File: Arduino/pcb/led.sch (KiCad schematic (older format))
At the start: 0 parts

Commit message: pcb: continue wiring / move parts to hierachival sheets
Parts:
- added C4: 100nF, symbol Device:C
- added D1: LED_RGB, symbol Device:LED_RGB
- added U2: 74HC595, SMD_Packages:SO-16-N, symbol floppyorgel-rescue:74HC595-74xx
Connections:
- new net: D1.4 (BA), U2.2 (QC)
- new net: D1.5 (GA), U2.1 (QB)
- new net: D1.6 (RA), U2.15 (QA)
- new net GND: C4.2, D1.1 (RK), D1.2 (GK), D1.3 (BK), U2.13 (G), U2.8 (GND)
- new net LATCH_LED: U2.12 (RCLK)
- new net MOSI: U2.14 (SER)
- new net SCK: U2.11 (SRCLK)
- new net VCC: C4.1, U2.10 (SRCLR), U2.16 (VCC)
- no-connect marks 0 -> 6
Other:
- note added: "Bypass"
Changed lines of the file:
@@
 $Descr A4 11693 8268
 encoding utf-8
-Sheet 1 6
+Sheet 5 6
 Title ""
 Date ""
@@
 Comment4 ""
 $EndDescr
+$Comp
+L power:VCC #PWR022
+U 1 1 5D09B29E
+P 5175 2850
+F 0 "#PWR022" H 5175 2700 50  0001 C CNN
+F 1 "VCC" H 5192 3023 50  0000 C CNN
+F 2 "" H 5175 2850 50  0001 C CNN
+F 3 "" H 5175 2850 50  0001 C CNN
+	1    5175 2850
+	1    0    0    -1
+$EndComp
+$Comp
+L power:GND #PWR023
+U 1 1 5D09B2A4
+P 5175 3950
+F 0 "#PWR023" H 5175 3700 50  0001 C CNN
+F 1 "GND" H 5180 3777 50  0000 C CNN
+F 2 "" H 5175 3950 50  0001 C CNN
+F 3 "" H 5175 3950 50  0001 C CNN
+	1    5175 3950
+	1    0    0    -1
+$EndComp
+$Comp
+L Device:LED_RGB D1
+U 1 1 5D09B2AA
+P 6700 3050
+F 0 "D1" H 6700 3547 50  0000 C CNN
+F 1 "LED_RGB" H 6700 3456 50  0000 C CNN
+F 2 "" H 6700 3000 50  0001 C CNN
+F 3 "~" H 6700 3000 50  0001 C CNN
+	1    6700 3050
+	-1   0    0    -1
+$EndComp
+$Comp
+L power:GND #PWR024
+U 1 1 5D09B2B0
+P 6900 3625
+F 0 "#PWR024" H 6900 3375 50  0001 C CNN
+F 1 "GND" H 6905 3452 50  0000 C CNN
+F 2 "" H 6900 3625 50  0001 C CNN
+F 3 "" H 6900 3625 50  0001 C CNN
+	1    6900 3625
+	1    0    0    -1
+$EndComp
+Wire Wire Line
+	6175 2950 6500 2950
+Wire Wire Line
+	6175 3050 6500 3050
+Connection ~ 6900 3050
+Connection ~ 6900 3250
+Wire Wire Line
+	6500 2950 6500 2850
+Wire Wire Line
+	6900 3050 6900 3250
+Wire Wire Line
+	6900 3250 6900 3625
+Wire Wire Line
+	6500 3150 6500 3250
+Wire Wire Line
+	6175 3150 6500 3150
+Wire Wire Line
+	6900 2850 6900 3050
+$Comp
+L power:GND #PWR021
+U 1 1 5D09B2C0
+P 4775 3550
+F 0 "#PWR021" H 4775 3300 50  0001 C CNN
+F 1 "GND" H 4780 3377 50  0000 C CNN
+F 2 "" H 4775 3550 50  0001 C CNN
+F 3 "" H 4775 3550 50  0001 C CNN
+	1    4775 3550
+	1    0    0    -1
+$EndComp
+Wire Wire Line
+	4775 3250 4375 3250
+$Comp
+L power:VCC #PWR020
+U 1 1 5D09B2C7
+P 4375 2850
+F 0 "#PWR020" H 4375 2700 50  0001 C CNN
+F 1 "VCC" H 4392 3023 50  0000 C CNN
+F 2 "" H 4375 2850 50  0001 C CNN
+F 3 "" H 4375 2850 50  0001 C CNN
+	1    4375 2850
+	1    0    0    -1
+$EndComp
+NoConn ~ 6175 3250
+NoConn ~ 6175 3350
+NoConn ~ 6175 3450
+NoConn ~ 6175 3550
+NoConn ~ 6175 3650
+NoConn ~ 6175 3850
+$Comp
+L floppyorgel-rescue:74HC595-74xx U2
+U 1 1 5D09B2D3
+P 5475 3400
+F 0 "U2" H 5625 4000 50  0000 C CNN
+F 1 "74HC595" H 5475 2800 50  0000 C CNN
+F 2 "SMD_Packages:SO-16-N" H 5475 3400 50  0001 C CNN
+F 3 "" H 5475 3400 50  0001 C CNN
+	1    5475 3400
+	1    0    0    -1
+$EndComp
+Wire Wire Line
+	4375 2850 4375 3250
+Text HLabel 4775 2950 0    50   Input ~ 0
+MOSI
+Text HLabel 4775 3150 0    50   Input ~ 0
+SCK
+Text HLabel 4775 3450 0    50   Input ~ 0
+LATCH_LED
+$Comp
+L Device:C C?
+U 1 1 5D18829B
+P 3750 3275
+AR Path="/5D18829B" Ref="C?"  Part="1"
+AR Path="/5CCFEC3E/5D18829B" Ref="C?"  Part="1"
+AR Path="/5CD3FBA6/5D18829B" Ref="C4"  Part="1"
+F 0 "C4" H 3525 3475 50  0000 L CNN
+F 1 "100nF" H 3475 3375 50  0000 L CNN
+F 2 "" H 3788 3125 50  0001 C CNN
+F 3 "~" H 3750 3275 50  0001 C CNN
+	1    3750 3275
+	1    0    0    -1
+$EndComp
+$Comp
+L power:VCC #PWR?
+U 1 1 5D1882A1
+P 3750 3000
+AR Path="/5CCFEC3E/5D1882A1" Ref="#PWR?"  Part="1"
+AR Path="/5CD3FBA6/5D1882A1" Ref="#PWR018"  Part="1"
+F 0 "#PWR018" H 3750 2850 50  0001 C CNN
+F 1 "VCC" H 3767 3173 50  0000 C CNN
+F 2 "" H 3750 3000 50  0001 C CNN
+F 3 "" H 3750 3000 50  0001 C CNN
+	1    3750 3000
+	1    0    0    -1
+$EndComp
+$Comp
+L power:GND #PWR?
+U 1 1 5D1882A7
+P 3750 3525
+AR Path="/5CCFEC3E/5D1882A7" Ref="#PWR?"  Part="1"
+AR Path="/5CD3FBA6/5D1882A7" Ref="#PWR019"  Part="1"
+F 0 "#PWR019" H 3750 3275 50  0001 C CNN
+F 1 "GND" H 3755 3352 50  0000 C CNN
+F 2 "" H 3750 3525 50  0001 C CNN
+F 3 "" H 3750 3525 50  0001 C CNN
+	1    3750 3525
+	1    0    0    -1
+$EndComp
+Wire Wire Line
+	3750 3000 3750 3125
+Wire Wire Line
+	3750 3425 3750 3525
+Text Notes 3375 2950 0    50   ~ 0
+Bypass
 $EndSCHEMATC

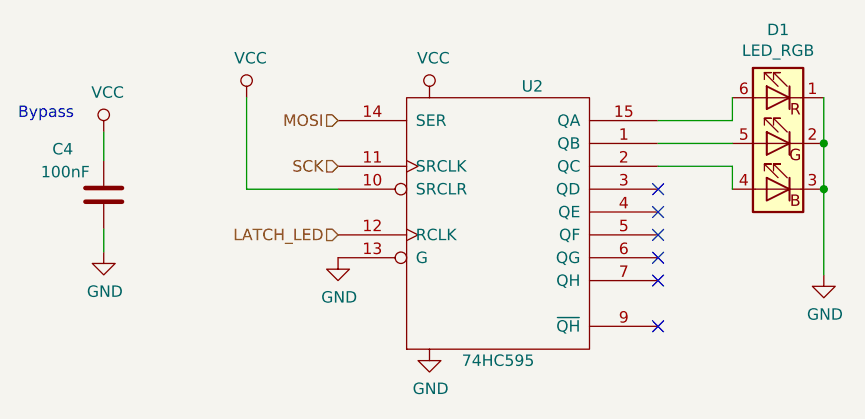
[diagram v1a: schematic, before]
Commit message: pcb: finish wiring / use ws2812 under chip led
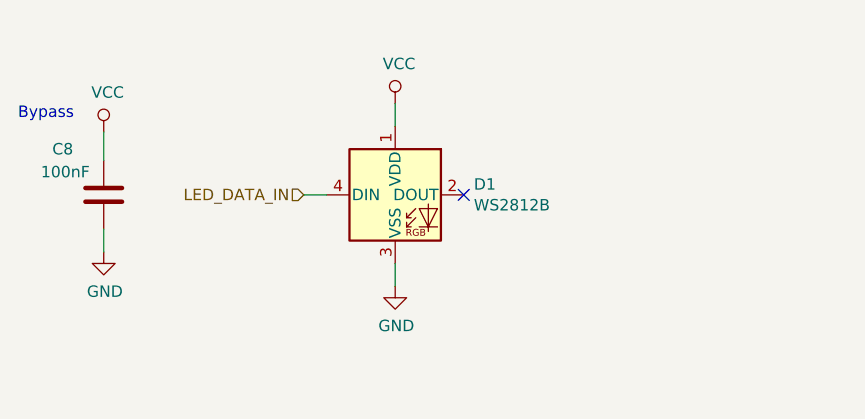
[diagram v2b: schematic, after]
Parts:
- removed D1: LED_RGB, symbol Device:LED_RGB
- removed U2: 74HC595, SMD_Packages:SO-16-N, symbol floppyorgel-rescue:74HC595-74xx
- added D1: WS2812B, LED_SMD:LED_WS2812B_PLCC4_5.0x5.0mm_P3.2mm, symbol LED:WS2812B
- renumbered C4 to C8
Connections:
- net GND: now also D1.3 (VSS)
- net VCC: now also D1.1 (VDD)
- new net LED_DATA_IN: D1.4 (DIN)
- no-connect marks 6 -> 1
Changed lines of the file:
@@
 $Descr A4 11693 8268
 encoding utf-8
-Sheet 5 6
+Sheet 6 6
 Title ""
 Date ""
@@
 $EndDescr
 $Comp
-L power:VCC #PWR022
-U 1 1 5D09B29E
-P 5175 2850
-F 0 "#PWR022" H 5175 2700 50  0001 C CNN
-F 1 "VCC" H 5192 3023 50  0000 C CNN
-F 2 "" H 5175 2850 50  0001 C CNN
-F 3 "" H 5175 2850 50  0001 C CNN
-	1    5175 2850
-	1    0    0    -1
-$EndComp
-$Comp
-L power:GND #PWR023
-U 1 1 5D09B2A4
-P 5175 3950
-F 0 "#PWR023" H 5175 3700 50  0001 C CNN
-F 1 "GND" H 5180 3777 50  0000 C CNN
-F 2 "" H 5175 3950 50  0001 C CNN
-F 3 "" H 5175 3950 50  0001 C CNN
-	1    5175 3950
-	1    0    0    -1
-$EndComp
-$Comp
-L Device:LED_RGB D1
-U 1 1 5D09B2AA
-P 6700 3050
-F 0 "D1" H 6700 3547 50  0000 C CNN
-F 1 "LED_RGB" H 6700 3456 50  0000 C CNN
-F 2 "" H 6700 3000 50  0001 C CNN
-F 3 "~" H 6700 3000 50  0001 C CNN
-	1    6700 3050
-	-1   0    0    -1
-$EndComp
-$Comp
-L power:GND #PWR024
-U 1 1 5D09B2B0
-P 6900 3625
-F 0 "#PWR024" H 6900 3375 50  0001 C CNN
-F 1 "GND" H 6905 3452 50  0000 C CNN
-F 2 "" H 6900 3625 50  0001 C CNN
-F 3 "" H 6900 3625 50  0001 C CNN
-	1    6900 3625
-	1    0    0    -1
-$EndComp
-Wire Wire Line
-	6175 2950 6500 2950
-Wire Wire Line
-	6175 3050 6500 3050
-Connection ~ 6900 3050
-Connection ~ 6900 3250
-Wire Wire Line
-	6500 2950 6500 2850
-Wire Wire Line
-	6900 3050 6900 3250
-Wire Wire Line
-	6900 3250 6900 3625
-Wire Wire Line
-	6500 3150 6500 3250
-Wire Wire Line
-	6175 3150 6500 3150
-Wire Wire Line
-	6900 2850 6900 3050
-$Comp
-L power:GND #PWR021
-U 1 1 5D09B2C0
-P 4775 3550
-F 0 "#PWR021" H 4775 3300 50  0001 C CNN
-F 1 "GND" H 4780 3377 50  0000 C CNN
-F 2 "" H 4775 3550 50  0001 C CNN
-F 3 "" H 4775 3550 50  0001 C CNN
-	1    4775 3550
-	1    0    0    -1
-$EndComp
-Wire Wire Line
-	4775 3250 4375 3250
-$Comp
-L power:VCC #PWR020
-U 1 1 5D09B2C7
-P 4375 2850
-F 0 "#PWR020" H 4375 2700 50  0001 C CNN
-F 1 "VCC" H 4392 3023 50  0000 C CNN
-F 2 "" H 4375 2850 50  0001 C CNN
-F 3 "" H 4375 2850 50  0001 C CNN
-	1    4375 2850
-	1    0    0    -1
-$EndComp
-NoConn ~ 6175 3250
-NoConn ~ 6175 3350
-NoConn ~ 6175 3450
-NoConn ~ 6175 3550
-NoConn ~ 6175 3650
-NoConn ~ 6175 3850
-$Comp
-L floppyorgel-rescue:74HC595-74xx U2
-U 1 1 5D09B2D3
-P 5475 3400
-F 0 "U2" H 5625 4000 50  0000 C CNN
-F 1 "74HC595" H 5475 2800 50  0000 C CNN
-F 2 "SMD_Packages:SO-16-N" H 5475 3400 50  0001 C CNN
-F 3 "" H 5475 3400 50  0001 C CNN
-	1    5475 3400
-	1    0    0    -1
-$EndComp
-Wire Wire Line
-	4375 2850 4375 3250
-Text HLabel 4775 2950 0    50   Input ~ 0
-MOSI
-Text HLabel 4775 3150 0    50   Input ~ 0
-SCK
-Text HLabel 4775 3450 0    50   Input ~ 0
-LATCH_LED
-$Comp
 L Device:C C?
 U 1 1 5D18829B
@@
 AR Path="/5D18829B" Ref="C?"  Part="1"
 AR Path="/5CCFEC3E/5D18829B" Ref="C?"  Part="1"
-AR Path="/5CD3FBA6/5D18829B" Ref="C4"  Part="1"
-F 0 "C4" H 3525 3475 50  0000 L CNN
+AR Path="/5CD3FBA6/5D18829B" Ref="C8"  Part="1"
+F 0 "C8" H 3525 3475 50  0000 L CNN
 F 1 "100nF" H 3475 3375 50  0000 L CNN
 F 2 "" H 3788 3125 50  0001 C CNN
@@
 P 3750 3000
 AR Path="/5CCFEC3E/5D1882A1" Ref="#PWR?"  Part="1"
-AR Path="/5CD3FBA6/5D1882A1" Ref="#PWR018"  Part="1"
-F 0 "#PWR018" H 3750 2850 50  0001 C CNN
+AR Path="/5CD3FBA6/5D1882A1" Ref="#PWR027"  Part="1"
+F 0 "#PWR027" H 3750 2850 50  0001 C CNN
 F 1 "VCC" H 3767 3173 50  0000 C CNN
 F 2 "" H 3750 3000 50  0001 C CNN
@@
 P 3750 3525
 AR Path="/5CCFEC3E/5D1882A7" Ref="#PWR?"  Part="1"
-AR Path="/5CD3FBA6/5D1882A7" Ref="#PWR019"  Part="1"
-F 0 "#PWR019" H 3750 3275 50  0001 C CNN
+AR Path="/5CD3FBA6/5D1882A7" Ref="#PWR028"  Part="1"
+F 0 "#PWR028" H 3750 3275 50  0001 C CNN
 F 1 "GND" H 3755 3352 50  0000 C CNN
 F 2 "" H 3750 3525 50  0001 C CNN
@@
 Text Notes 3375 2950 0    50   ~ 0
 Bypass
+$Comp
+L LED:WS2812B D1
+U 1 1 5CC4A8E5
+P 5025 3275
+F 0 "D1" H 5369 3321 50  0000 L CNN
+F 1 "WS2812B" H 5369 3230 50  0000 L CNN
+F 2 "LED_SMD:LED_WS2812B_PLCC4_5.0x5.0mm_P3.2mm" H 5075 2975 50  0001 L TNN
+F 3 "https://cdn-shop.adafruit.com/datasheets/WS2812B.pdf" H 5125 2900 50  0001 L TNN
+	1    5025 3275
+	1    0    0    -1
+$EndComp
+$Comp
+L power:VCC #PWR?
+U 1 1 5CC4D6AB
+P 5025 2875
+AR Path="/5CCFEC3E/5CC4D6AB" Ref="#PWR?"  Part="1"
+AR Path="/5CD3FBA6/5CC4D6AB" Ref="#PWR029"  Part="1"
+F 0 "#PWR029" H 5025 2725 50  0001 C CNN
+F 1 "VCC" H 5042 3048 50  0000 C CNN
+F 2 "" H 5025 2875 50  0001 C CNN
+F 3 "" H 5025 2875 50  0001 C CNN
+	1    5025 2875
+	1    0    0    -1
+$EndComp
+Wire Wire Line
+	5025 2875 5025 2975
+$Comp
+L power:GND #PWR030
+U 1 1 5CC4FADA
+P 5025 3675
+F 0 "#PWR030" H 5025 3425 50  0001 C CNN
+F 1 "GND" H 5030 3502 50  0000 C CNN
+F 2 "" H 5025 3675 50  0001 C CNN
+F 3 "" H 5025 3675 50  0001 C CNN
+	1    5025 3675
+	1    0    0    -1
+$EndComp
+Wire Wire Line
+	5025 3575 5025 3675
+Text HLabel 4625 3275 0    50   Input ~ 0
+LED_DATA_IN
+Wire Wire Line
+	4625 3275 4725 3275
+NoConn ~ 5325 3275
 $EndSCHEMATC

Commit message: pcb: assign footprints
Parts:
- C8: footprint (none) -> Capacitor_SMD:C_0201_0603Metric
- D1: footprint LED_SMD:LED_WS2812B_PLCC4_5.0x5.0mm_P3.2mm -> LED_SMD:LED_RGB_1210
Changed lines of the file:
@@
 F 0 "C8" H 3525 3475 50  0000 L CNN
 F 1 "100nF" H 3475 3375 50  0000 L CNN
-F 2 "" H 3788 3125 50  0001 C CNN
+F 2 "Capacitor_SMD:C_0201_0603Metric" H 3788 3125 50  0001 C CNN
 F 3 "~" H 3750 3275 50  0001 C CNN
 	1    3750 3275
@@
 F 0 "D1" H 5369 3321 50  0000 L CNN
 F 1 "WS2812B" H 5369 3230 50  0000 L CNN
-F 2 "LED_SMD:LED_WS2812B_PLCC4_5.0x5.0mm_P3.2mm" H 5075 2975 50  0001 L TNN
+F 2 "LED_SMD:LED_RGB_1210" H 5075 2975 50  0001 L TNN
 F 3 "https://cdn-shop.adafruit.com/datasheets/WS2812B.pdf" H 5125 2900 50  0001 L TNN
 	1    5025 3275

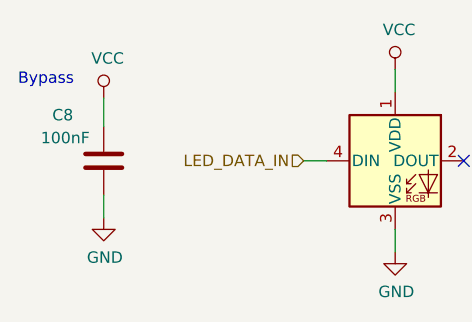
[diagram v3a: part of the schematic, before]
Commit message: pcb: add I2C eeprom
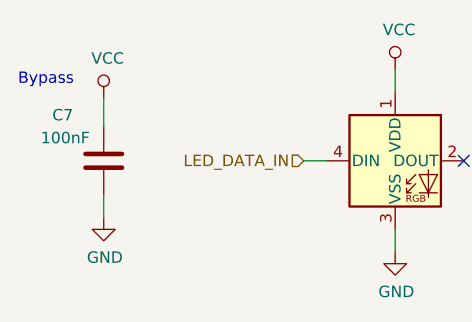
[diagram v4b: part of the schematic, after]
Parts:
- renumbered C8 to C7
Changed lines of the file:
@@
 AR Path="/5D18829B" Ref="C?"  Part="1"
 AR Path="/5CCFEC3E/5D18829B" Ref="C?"  Part="1"
-AR Path="/5CD3FBA6/5D18829B" Ref="C8"  Part="1"
-F 0 "C8" H 3525 3475 50  0000 L CNN
+AR Path="/5CD3FBA6/5D18829B" Ref="C7"  Part="1"
+F 0 "C7" H 3525 3475 50  0000 L CNN
 F 1 "100nF" H 3475 3375 50  0000 L CNN
 F 2 "Capacitor_SMD:C_0201_0603Metric" H 3788 3125 50  0001 C CNN
@@
 P 3750 3000
 AR Path="/5CCFEC3E/5D1882A1" Ref="#PWR?"  Part="1"
-AR Path="/5CD3FBA6/5D1882A1" Ref="#PWR027"  Part="1"
-F 0 "#PWR027" H 3750 2850 50  0001 C CNN
+AR Path="/5CD3FBA6/5D1882A1" Ref="#PWR030"  Part="1"
+F 0 "#PWR030" H 3750 2850 50  0001 C CNN
 F 1 "VCC" H 3767 3173 50  0000 C CNN
 F 2 "" H 3750 3000 50  0001 C CNN
@@
 P 3750 3525
 AR Path="/5CCFEC3E/5D1882A7" Ref="#PWR?"  Part="1"
-AR Path="/5CD3FBA6/5D1882A7" Ref="#PWR028"  Part="1"
-F 0 "#PWR028" H 3750 3275 50  0001 C CNN
+AR Path="/5CD3FBA6/5D1882A7" Ref="#PWR031"  Part="1"
+F 0 "#PWR031" H 3750 3275 50  0001 C CNN
 F 1 "GND" H 3755 3352 50  0000 C CNN
 F 2 "" H 3750 3525 50  0001 C CNN
@@
 P 5025 2875
 AR Path="/5CCFEC3E/5CC4D6AB" Ref="#PWR?"  Part="1"
-AR Path="/5CD3FBA6/5CC4D6AB" Ref="#PWR029"  Part="1"
-F 0 "#PWR029" H 5025 2725 50  0001 C CNN
+AR Path="/5CD3FBA6/5CC4D6AB" Ref="#PWR032"  Part="1"
+F 0 "#PWR032" H 5025 2725 50  0001 C CNN
 F 1 "VCC" H 5042 3048 50  0000 C CNN
 F 2 "" H 5025 2875 50  0001 C CNN
@@
 	5025 2875 5025 2975
 $Comp
-L power:GND #PWR030
+L power:GND #PWR033
 U 1 1 5CC4FADA
 P 5025 3675
-F 0 "#PWR030" H 5025 3425 50  0001 C CNN
+F 0 "#PWR033" H 5025 3425 50  0001 C CNN
 F 1 "GND" H 5030 3502 50  0000 C CNN
 F 2 "" H 5025 3675 50  0001 C CNN

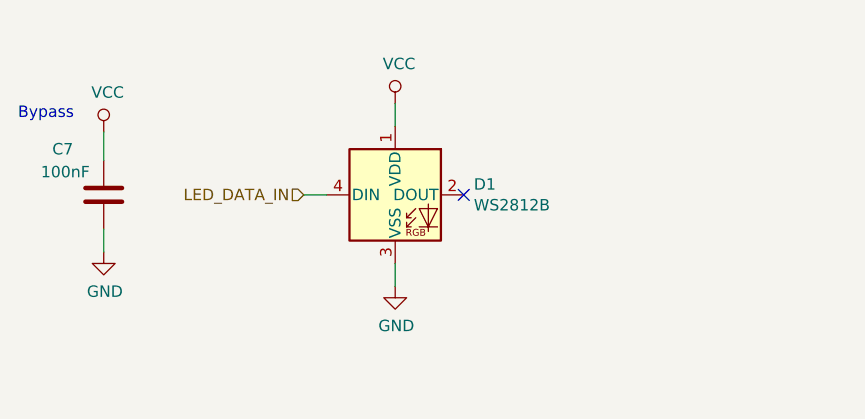
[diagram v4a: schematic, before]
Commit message: pcb: continue placement + add some info on silk
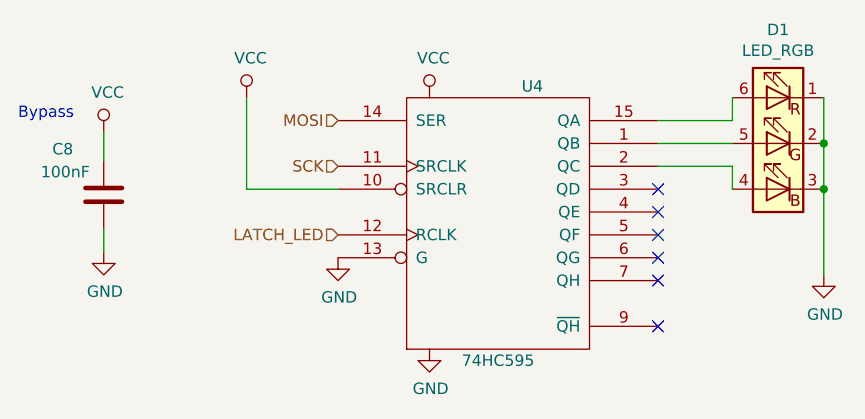
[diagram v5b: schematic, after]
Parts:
- removed D1: WS2812B, LED_SMD:LED_RGB_1210, symbol LED:WS2812B
- added D1: LED_RGB, LED_SMD:LED_RGB_1210, symbol Device:LED_RGB
- added U4: 74HC595, Package_SO:TSSOP-16_4.4x5mm_P0.65mm, symbol floppyorgel-rescue:74HC595-74xx
- C8: renamed from C7; footprint Capacitor_SMD:C_0201_0603Metric -> Capacitor_SMD:C_0805_2012Metric
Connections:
- net GND: now also D1.1 (RK), D1.2 (GK), D1.3 (BK), U4.13 (G), U4.8 (GND)
- net VCC: now also U4.10 (SRCLR), U4.16 (VCC)
- new net: D1.4 (BA), U4.2 (QC)
- new net: D1.5 (GA), U4.1 (QB)
- new net: D1.6 (RA), U4.15 (QA)
- new net LATCH_LED: U4.12 (RCLK)
- new net MOSI: U4.14 (SER)
- new net SCK: U4.11 (SRCLK)
- no-connect marks 1 -> 6
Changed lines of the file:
@@
 $EndDescr
+$Comp
+L power:VCC #PWR037
+U 1 1 5D09B29E
+P 5175 2850
+F 0 "#PWR037" H 5175 2700 50  0001 C CNN
+F 1 "VCC" H 5192 3023 50  0000 C CNN
+F 2 "" H 5175 2850 50  0001 C CNN
+F 3 "" H 5175 2850 50  0001 C CNN
+	1    5175 2850
+	1    0    0    -1
+$EndComp
+$Comp
+L power:GND #PWR038
+U 1 1 5D09B2A4
+P 5175 3950
+F 0 "#PWR038" H 5175 3700 50  0001 C CNN
+F 1 "GND" H 5180 3777 50  0000 C CNN
+F 2 "" H 5175 3950 50  0001 C CNN
+F 3 "" H 5175 3950 50  0001 C CNN
+	1    5175 3950
+	1    0    0    -1
+$EndComp
+$Comp
+L Device:LED_RGB D1
+U 1 1 5D09B2AA
+P 6700 3050
+F 0 "D1" H 6700 3547 50  0000 C CNN
+F 1 "LED_RGB" H 6700 3456 50  0000 C CNN
+F 2 "LED_SMD:LED_RGB_1210" H 6700 3000 50  0001 C CNN
+F 3 "~" H 6700 3000 50  0001 C CNN
+	1    6700 3050
+	-1   0    0    -1
+$EndComp
+$Comp
+L power:GND #PWR039
+U 1 1 5D09B2B0
+P 6900 3625
+F 0 "#PWR039" H 6900 3375 50  0001 C CNN
+F 1 "GND" H 6905 3452 50  0000 C CNN
+F 2 "" H 6900 3625 50  0001 C CNN
+F 3 "" H 6900 3625 50  0001 C CNN
+	1    6900 3625
+	1    0    0    -1
+$EndComp
+Wire Wire Line
+	6175 2950 6500 2950
+Wire Wire Line
+	6175 3050 6500 3050
+Connection ~ 6900 3050
+Connection ~ 6900 3250
+Wire Wire Line
+	6500 2950 6500 2850
+Wire Wire Line
+	6900 3050 6900 3250
+Wire Wire Line
+	6900 3250 6900 3625
+Wire Wire Line
+	6500 3150 6500 3250
+Wire Wire Line
+	6175 3150 6500 3150
+Wire Wire Line
+	6900 2850 6900 3050
+$Comp
+L power:GND #PWR036
+U 1 1 5D09B2C0
+P 4775 3550
+F 0 "#PWR036" H 4775 3300 50  0001 C CNN
+F 1 "GND" H 4780 3377 50  0000 C CNN
+F 2 "" H 4775 3550 50  0001 C CNN
+F 3 "" H 4775 3550 50  0001 C CNN
+	1    4775 3550
+	1    0    0    -1
+$EndComp
+Wire Wire Line
+	4775 3250 4375 3250
+$Comp
+L power:VCC #PWR035
+U 1 1 5D09B2C7
+P 4375 2850
+F 0 "#PWR035" H 4375 2700 50  0001 C CNN
+F 1 "VCC" H 4392 3023 50  0000 C CNN
+F 2 "" H 4375 2850 50  0001 C CNN
+F 3 "" H 4375 2850 50  0001 C CNN
+	1    4375 2850
+	1    0    0    -1
+$EndComp
+NoConn ~ 6175 3250
+NoConn ~ 6175 3350
+NoConn ~ 6175 3450
+NoConn ~ 6175 3550
+NoConn ~ 6175 3650
+NoConn ~ 6175 3850
+$Comp
+L floppyorgel-rescue:74HC595-74xx U4
+U 1 1 5D09B2D3
+P 5475 3400
+F 0 "U4" H 5625 4000 50  0000 C CNN
+F 1 "74HC595" H 5475 2800 50  0000 C CNN
+F 2 "Package_SO:TSSOP-16_4.4x5mm_P0.65mm" H 5475 3400 50  0001 C CNN
+F 3 "" H 5475 3400 50  0001 C CNN
+	1    5475 3400
+	1    0    0    -1
+$EndComp
+Wire Wire Line
+	4375 2850 4375 3250
+Text HLabel 4775 2950 0    50   Input ~ 0
+MOSI
+Text HLabel 4775 3150 0    50   Input ~ 0
+SCK
+Text HLabel 4775 3450 0    50   Input ~ 0
+LATCH_LED
 $Comp
 L Device:C C?
@@
 AR Path="/5D18829B" Ref="C?"  Part="1"
 AR Path="/5CCFEC3E/5D18829B" Ref="C?"  Part="1"
-AR Path="/5CD3FBA6/5D18829B" Ref="C7"  Part="1"
-F 0 "C7" H 3525 3475 50  0000 L CNN
+AR Path="/5CD3FBA6/5D18829B" Ref="C8"  Part="1"
+F 0 "C8" H 3525 3475 50  0000 L CNN
 F 1 "100nF" H 3475 3375 50  0000 L CNN
-F 2 "Capacitor_SMD:C_0201_0603Metric" H 3788 3125 50  0001 C CNN
+F 2 "Capacitor_SMD:C_0805_2012Metric" H 3788 3125 50  0001 C CNN
 F 3 "~" H 3750 3275 50  0001 C CNN
 	1    3750 3275
@@
 P 3750 3000
 AR Path="/5CCFEC3E/5D1882A1" Ref="#PWR?"  Part="1"
-AR Path="/5CD3FBA6/5D1882A1" Ref="#PWR030"  Part="1"
-F 0 "#PWR030" H 3750 2850 50  0001 C CNN
+AR Path="/5CD3FBA6/5D1882A1" Ref="#PWR033"  Part="1"
+F 0 "#PWR033" H 3750 2850 50  0001 C CNN
 F 1 "VCC" H 3767 3173 50  0000 C CNN
 F 2 "" H 3750 3000 50  0001 C CNN
@@
 P 3750 3525
 AR Path="/5CCFEC3E/5D1882A7" Ref="#PWR?"  Part="1"
-AR Path="/5CD3FBA6/5D1882A7" Ref="#PWR031"  Part="1"
-F 0 "#PWR031" H 3750 3275 50  0001 C CNN
+AR Path="/5CD3FBA6/5D1882A7" Ref="#PWR034"  Part="1"
+F 0 "#PWR034" H 3750 3275 50  0001 C CNN
 F 1 "GND" H 3755 3352 50  0000 C CNN
 F 2 "" H 3750 3525 50  0001 C CNN
@@
 Text Notes 3375 2950 0    50   ~ 0
 Bypass
-$Comp
-L LED:WS2812B D1
-U 1 1 5CC4A8E5
-P 5025 3275
-F 0 "D1" H 5369 3321 50  0000 L CNN
-F 1 "WS2812B" H 5369 3230 50  0000 L CNN
-F 2 "LED_SMD:LED_RGB_1210" H 5075 2975 50  0001 L TNN
-F 3 "https://cdn-shop.adafruit.com/datasheets/WS2812B.pdf" H 5125 2900 50  0001 L TNN
-	1    5025 3275
-	1    0    0    -1
-$EndComp
-$Comp
-L power:VCC #PWR?
-U 1 1 5CC4D6AB
-P 5025 2875
-AR Path="/5CCFEC3E/5CC4D6AB" Ref="#PWR?"  Part="1"
-AR Path="/5CD3FBA6/5CC4D6AB" Ref="#PWR032"  Part="1"
-F 0 "#PWR032" H 5025 2725 50  0001 C CNN
-F 1 "VCC" H 5042 3048 50  0000 C CNN
-F 2 "" H 5025 2875 50  0001 C CNN
-F 3 "" H 5025 2875 50  0001 C CNN
-	1    5025 2875
-	1    0    0    -1
-$EndComp
-Wire Wire Line
-	5025 2875 5025 2975
-$Comp
-L power:GND #PWR033
-U 1 1 5CC4FADA
-P 5025 3675
-F 0 "#PWR033" H 5025 3425 50  0001 C CNN
-F 1 "GND" H 5030 3502 50  0000 C CNN
-F 2 "" H 5025 3675 50  0001 C CNN
-F 3 "" H 5025 3675 50  0001 C CNN
-	1    5025 3675
-	1    0    0    -1
-$EndComp
-Wire Wire Line
-	5025 3575 5025 3675
-Text HLabel 4625 3275 0    50   Input ~ 0
-LED_DATA_IN
-Wire Wire Line
-	4625 3275 4725 3275
-NoConn ~ 5325 3275
 $EndSCHEMATC
